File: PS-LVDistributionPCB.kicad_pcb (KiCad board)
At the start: 2 copper layers, 132.1 x 58.5 mm, 30 parts, among them J1 Conn_01x02, J10 Conn_01x02, J11 Conn_01x02, J12 Conn_01x02, J15 Conn_01x20, J2 Conn_01x02, J3 Conn_01x02, J4 Conn_01x02, J5 Conn_01x02, J6 Conn_01x02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

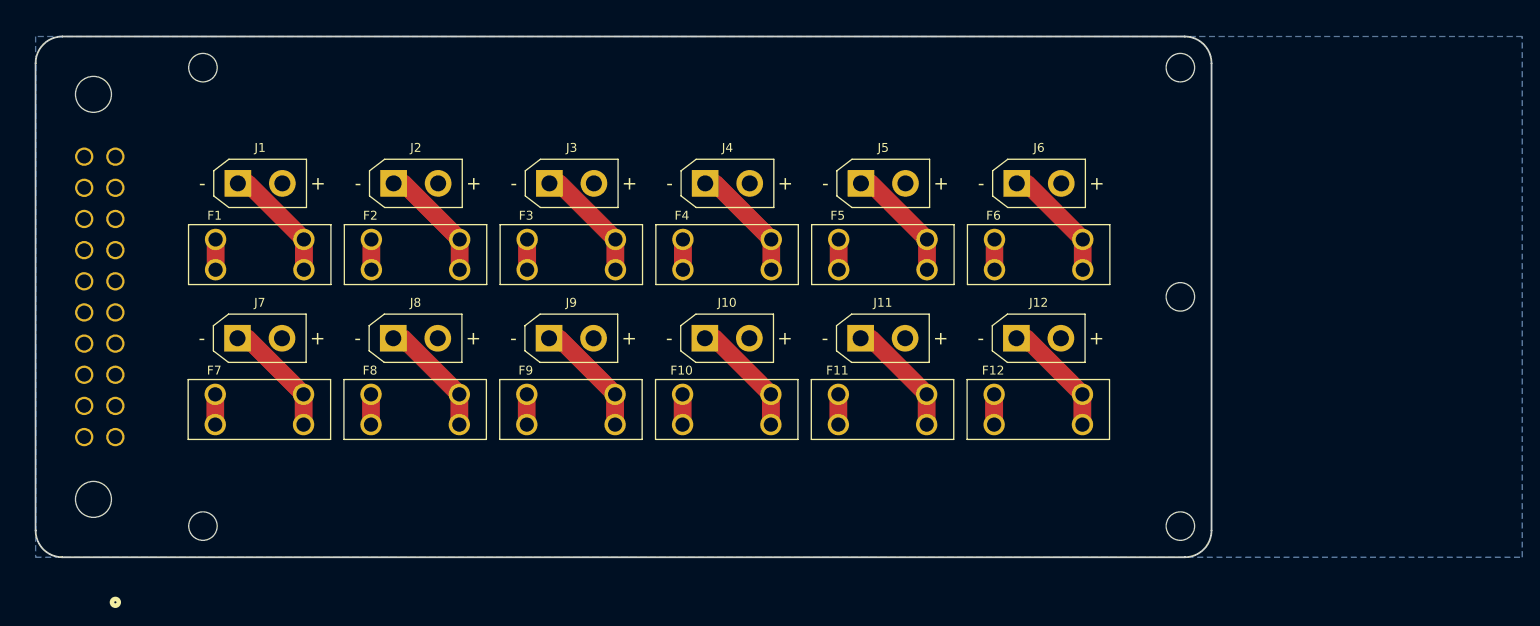
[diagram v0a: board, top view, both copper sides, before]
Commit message: added TVS diodes and routed traces
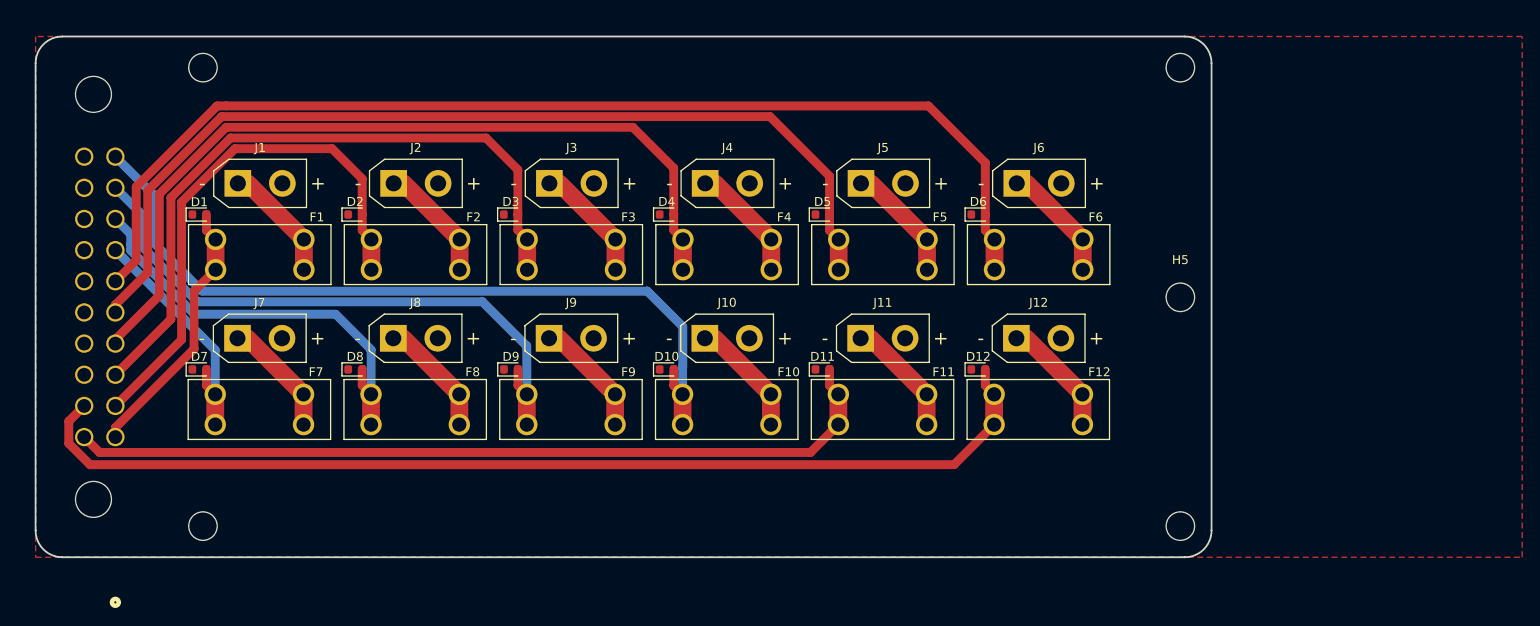
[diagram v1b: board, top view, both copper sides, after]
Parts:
- removed REF** (x5): MountingHole_3.2mm_M3, MountingHole:MountingHole_3.2mm_M3
- added D1: TVS, Diode_SMD:D_0603_1608Metric, F.Cu at (104.4, 78.0)
- added D10: TVS, Diode_SMD:D_0603_1608Metric, F.Cu at (156.9, 95.4)
- added D11: TVS, Diode_SMD:D_0603_1608Metric, F.Cu at (174.4, 95.4)
- added D12: TVS, Diode_SMD:D_0603_1608Metric, F.Cu at (191.9, 95.4)
- added D2: TVS, Diode_SMD:D_0603_1608Metric, F.Cu at (121.9, 78.0)
- added D3: TVS, Diode_SMD:D_0603_1608Metric, F.Cu at (139.4, 78.0)
- added D4: TVS, Diode_SMD:D_0603_1608Metric, F.Cu at (156.9, 78.0)
- added D5: TVS, Diode_SMD:D_0603_1608Metric, F.Cu at (174.4, 78.0)
- added D6: TVS, Diode_SMD:D_0603_1608Metric, F.Cu at (191.9, 78.0)
- added D7: TVS, Diode_SMD:D_0603_1608Metric, F.Cu at (104.4, 95.4)
- added D8: TVS, Diode_SMD:D_0603_1608Metric, F.Cu at (121.9, 95.4)
- added D9: TVS, Diode_SMD:D_0603_1608Metric, F.Cu at (139.4, 95.4)
- added H1: MountingHole, MountingHole:MountingHole_3.2mm_M3, F.Cu at (104.8, 61.5)
- added H2: MountingHole, MountingHole:MountingHole_3.2mm_M3, F.Cu at (214.6, 61.5)
- added H3: MountingHole, MountingHole:MountingHole_3.2mm_M3, F.Cu at (104.8, 113.0)
- added H4: MountingHole, MountingHole:MountingHole_3.2mm_M3, F.Cu at (214.6, 113.0)
- added H5: MountingHole, MountingHole:MountingHole_3.2mm_M3, F.Cu at (214.6, 87.3)
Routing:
- net P6: track 3.40 -> 125.8 mm
- net P12: track 3.40 -> 118.3 mm
- net P5: track 3.40 -> 108.9 mm
- net P4: track 3.40 -> 93.5 mm
- net P11: track 3.40 -> 93.3 mm
- net P10: track 3.40 -> 89.0 mm
- net P3: track 3.40 -> 77.4 mm
- net P9: track 3.40 -> 67.7 mm
- net P2: track 3.40 -> 60.8 mm
- net P8: track 3.40 -> 47.5 mm
- net P1: track 3.40 -> 30.1 mm
- net P7: track 3.40 -> 27.5 mm
- added copper zone on F.Cu, net GND
- removed copper zone on B.Cu, net GND

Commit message: 14 outputs with 2 row mx150 symbol
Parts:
- added D13: TVS, Diode_SMD:D_0603_1608Metric, F.Cu at (191.9, 95.4)
- added D14: TVS, Diode_SMD:D_0603_1608Metric, F.Cu at (209.4, 95.4)
- added F13: 3568, footprints:FUSE_3568, F.Cu at (198.6, 99.9)
- added F14: 3568, footprints:FUSE_3568, F.Cu at (216.1, 99.9)
- added J13: Conn_01x02, footprints:AMASS_XT30UPB-M_1x02_P5.0mm_Vertical, F.Cu at (196.2, 91.9)
- added J14: Conn_01x02, footprints:AMASS_XT30UPB-M_1x02_P5.0mm_Vertical, F.Cu at (213.7, 91.9)
- J15: value Conn_01x20 -> Conn_02x10_Top_Bottom
- moved F7 106.5 mm to (216.2, 82.5)
- moved J7 106.5 mm to (213.7, 74.5)
- moved D7 106.4 mm to (209.4, 78.0)
- moved D10 17.5 mm to (139.4, 95.4)
- moved D11 17.5 mm to (156.9, 95.4)
- moved D12 17.5 mm to (174.4, 95.4)
- moved D8 17.5 mm to (104.4, 95.4)
- moved D9 17.5 mm to (121.9, 95.4)
- moved F10 17.5 mm to (146.1, 99.9)
- moved F11 17.5 mm to (163.6, 99.9)
- moved F12 17.5 mm to (181.1, 99.9)
- moved F9 17.5 mm to (128.6, 99.9)
- moved J10 17.5 mm to (143.7, 91.9)
- moved J11 17.5 mm to (161.2, 91.9)
- moved J12 17.5 mm to (178.7, 91.9)
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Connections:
- J15 pad 13: GND -> P13
- J15 pad 14: GND -> P14
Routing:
- net P14: track 0.00 -> 155.1 mm
- net P13: track 0.00 -> 124.8 mm
- net P7: track 27.5 -> 140.3 mm
- net P10: track 89.0 -> 65.4 mm
- net P9: track 67.7 -> 46.5 mm
- net P12: track 118.3 -> 100.7 mm
- net P11: track 93.3 -> 75.8 mm
- net P8: track 47.5 -> 31.0 mm
- net Net-(J13-Pin_1): track 0.00 -> 13.5 mm
- net Net-(J14-Pin_1): track 0.00 -> 13.4 mm
- net P6: track 125.8 -> 121.4 mm
- net P4: track 93.5 -> 89.4 mm
- net P3: track 77.4 -> 73.4 mm
- net P5: track 108.9 -> 105.2 mm
- net P2: track 60.8 -> 57.4 mm
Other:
- board size 132.1 x 58.5 mm -> 146.2 x 58.5 mm

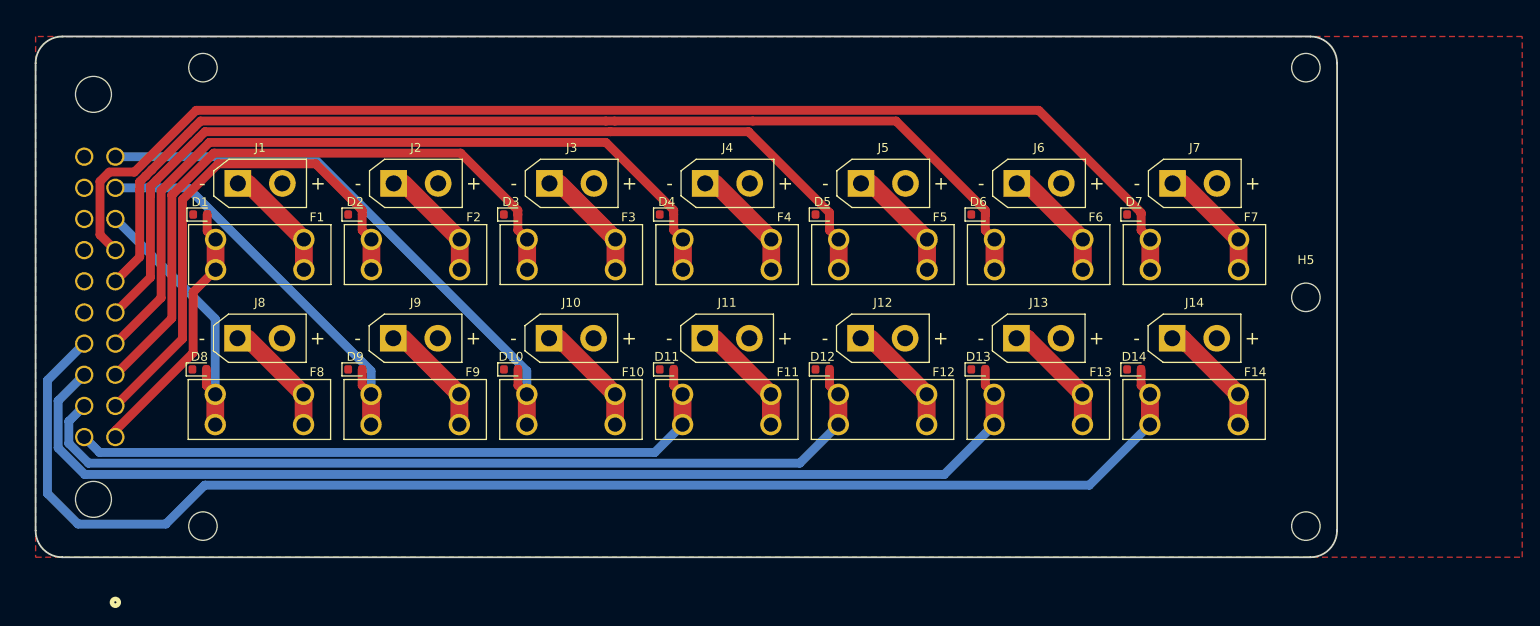
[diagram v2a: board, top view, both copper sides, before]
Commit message: widened board for ptn
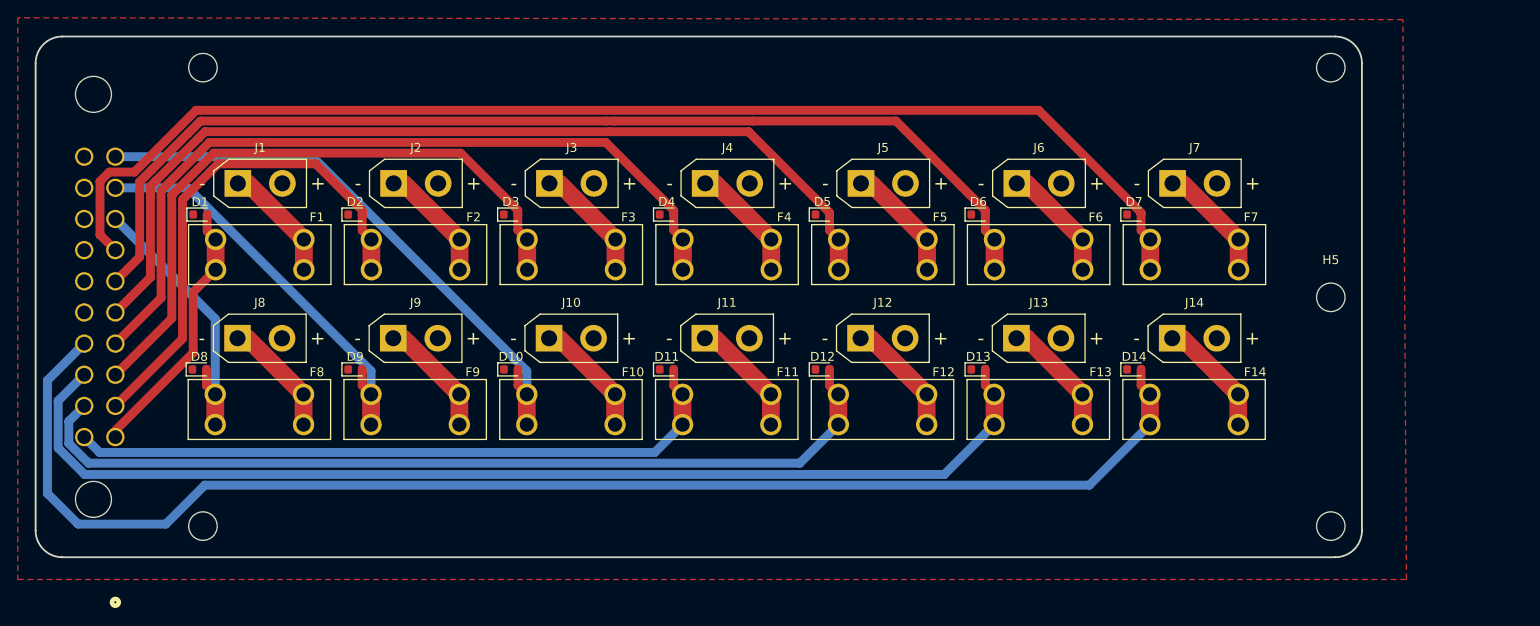
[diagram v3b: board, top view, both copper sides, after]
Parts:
- moved H2 2.80 mm to (231.5, 61.5)
- moved H4 2.80 mm to (231.5, 113.0)
- moved H5 2.80 mm to (231.5, 87.3)
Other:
- board size 146.2 x 58.5 mm -> 149 x 58.5 mm
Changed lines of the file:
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@@
 	(footprint "MountingHole:MountingHole_3.2mm_M3"
 		(layer "F.Cu")
-		(at 228.7 87.3)
+		(at 231.5 87.3)
 		(descr "Mounting Hole 3.2mm, no annular, M3")
 		(tags "mounting hole 3.2mm no annular m3")
@@
 	(footprint "MountingHole:MountingHole_3.2mm_M3"
 		(layer "F.Cu")
-		(at 228.7 61.5)
+		(at 231.5 61.5)
 		(descr "Mounting Hole 3.2mm, no annular, M3")
 		(tags "mounting hole 3.2mm no annular m3")
@@
 	(footprint "MountingHole:MountingHole_3.2mm_M3"
 		(layer "F.Cu")
-		(at 228.7 113)
+		(at 231.5 113)
 		(descr "Mounting Hole 3.2mm, no annular, M3")
 		(tags "mounting hole 3.2mm no annular m3")
@@
 	)
 	(gr_line
-		(start 229.2 116.5)
-		(end 89 116.5)
+		(start 235 61)
+		(end 235 113.5)
 		(stroke
 			(width 0.2)
@@
 		(layer "Edge.Cuts")
 	)
-	(gr_arc
-		(start 232.2 113.5)
-		(mid 231.32132 115.62132)
-		(end 229.2 116.5)
+	(gr_line
+		(start 89 58)
+		(end 232 58)
 		(stroke
 			(width 0.2)
@@
 		(layer "Edge.Cuts")
 	)
-	(gr_arc
-		(start 86 61)
-		(mid 86.87868 58.87868)
-		(end 89 58)
+	(gr_line
+		(start 86 113.5)
+		(end 86 61)
 		(stroke
 			(width 0.2)
@@
 	)
 	(gr_line
-		(start 232.2 61)
-		(end 232.2 113.5)
+		(start 232 116.5)
+		(end 89 116.5)
 		(stroke
 			(width 0.2)
@@
 		(layer "Edge.Cuts")
 	)
-	(gr_line
-		(start 86 113.5)
-		(end 86 61)
+	(gr_arc
+		(start 86 61)
+		(mid 86.87868 58.87868)
+		(end 89 58)
 		(stroke
 			(width 0.2)
@@
 		(layer "Edge.Cuts")
 	)
-	(gr_line
-		(start 89 58)
-		(end 229.2 58)
+	(gr_arc
+		(start 235 113.5)
+		(mid 234.12132 115.62132)
+		(end 232 116.5)
 		(stroke
 			(width 0.2)
@@
 	)
 	(gr_arc
-		(start 229.2 58)
-		(mid 231.32132 58.87868)
-		(end 232.2 61)
+		(start 232 58)
+		(mid 234.12132 58.87868)
+		(end 235 61)
 		(stroke
 			(width 0.2)
@@
 		(layer "F.Cu")
 		(hatch edge 0.5)
-		(connect_pads yes
+		(connect_pads
 			(clearance 0.5)
 		)
@@
 		(polygon
 			(pts
-				(xy 86 58) (xy 86 116.5) (xy 253 116.5) (xy 253 58)
+				(xy 84 55.9) (xy 84 119) (xy 240 119) (xy 239.6 56.1)
 			)
 		)
